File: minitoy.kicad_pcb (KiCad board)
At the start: 2 copper layers, 44 x 40 mm, 39 parts, among them J1 Conn_01x06, J2 PMOD1, J4 USB_B_Micro, J5 PMOD2, U1 ICE40UP5K-SG48, U2 ESP-12E, U3 MIC5504-3.3YM5, U4 MIC5504-1.2YM5, U5 MIC5504-3.3YM5

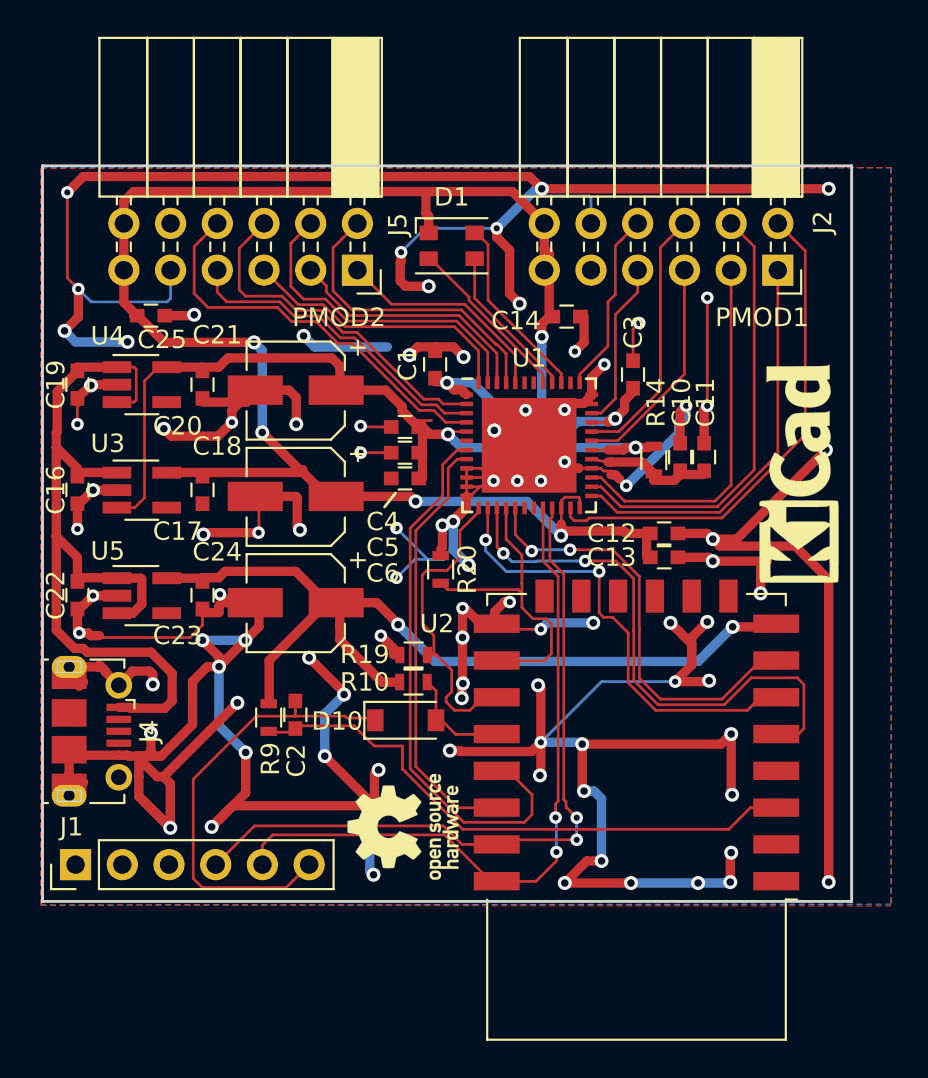
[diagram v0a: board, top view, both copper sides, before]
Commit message: v0.2: fix ESP POR straps and reset, fix typo on serial connector
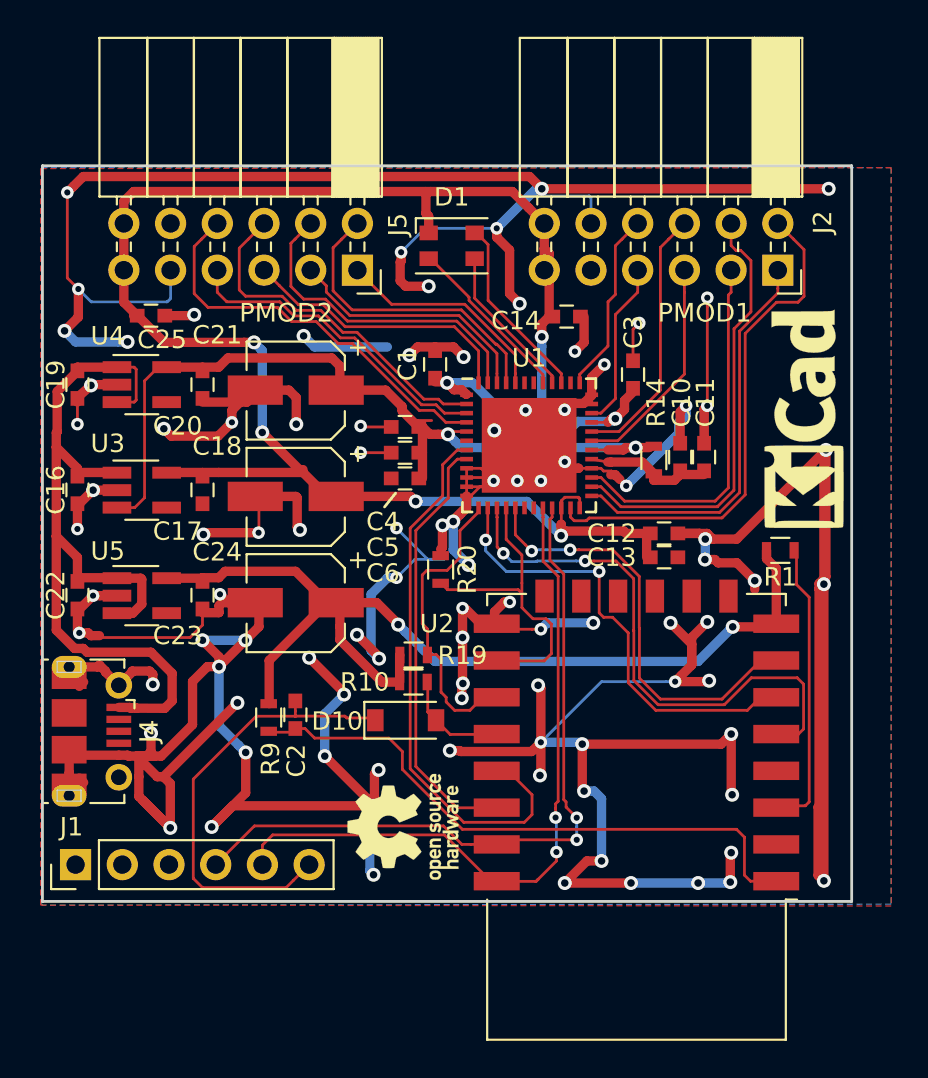
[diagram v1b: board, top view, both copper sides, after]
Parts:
- added R1: 10k, Resistors_SMD:R_0603, F.Cu at (131.1, 120.9)
- C2: value 0.1uF -> 1uF
- moved REF** 2.99 mm to (132.2, 113.8)
- turned R19 to 180 degrees
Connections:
- J1 pad 2: Net-(J1-Pad2) -> (no net)
- J1 pad 3: Net-(J1-Pad3) -> (no net)
- J4 pad 2: Net-(J4-Pad2) -> (no net)
- J4 pad 3: Net-(J4-Pad3) -> (no net)
- J4 pad 4: Net-(J4-Pad4) -> (no net)
- R19 pad 1: GND -> FPGA_INT
- R19 pad 2: FPGA_INT -> +3.3VA
- U1 pad 18: Net-(U1-Pad18) -> (no net)
- U1 pad 19: Net-(U1-Pad19) -> (no net)
- U1 pad 38: Net-(U1-Pad38) -> (no net)
- U1 pad 42: Net-(U1-Pad42) -> (no net)
- U1 pad 43: Net-(U1-Pad43) -> (no net)
- U1 pad 6: Net-(U1-Pad6) -> (no net)
- U2 pad 1: Net-(U2-Pad1) -> Net-(C2-Pad1)
- U2 pad 10: Net-(U2-Pad10) -> (no net)
- U2 pad 11: Net-(U2-Pad11) -> (no net)
- U2 pad 12: Net-(U2-Pad12) -> (no net)
- U2 pad 13: Net-(U2-Pad13) -> (no net)
- U2 pad 14: Net-(U2-Pad14) -> (no net)
- U2 pad 2: Net-(U2-Pad2) -> (no net)
- U2 pad 3: Net-(C2-Pad1) -> Net-(R1-Pad1)
- U2 pad 4: Net-(U2-Pad4) -> (no net)
- U2 pad 9: Net-(U2-Pad9) -> (no net)
- U3 pad 4: Net-(U3-Pad4) -> (no net)
- U4 pad 4: Net-(U4-Pad4) -> (no net)
- U5 pad 4: Net-(U5-Pad4) -> (no net)
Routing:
- net GND: track 407.2 -> 435.0 mm, vias 94 -> 96
- net Net-(R1-Pad1): track 0.00 -> 15.8 mm
- net +3.3VA: track 49.1 -> 54.9 mm
- net Net-(C2-Pad1): track 31.3 -> 32.8 mm
- net PMOD-1.7: track 27.4 -> 28.0 mm
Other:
- board text added: "a.litt 3/10/18"
- board text added: "minitoy v0.2"
- board text removed: "a.litt 2/22/18"
- board text removed: "minitoy v0.1"
